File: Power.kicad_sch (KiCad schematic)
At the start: 74 parts, among them J10 Conn_01x02_Socket, J12 USB_C_Receptacle_USB2.0_14P, J22 Conn_01x02_Socket, J23 Conn_01x02_Socket, J24 Conn_01x02_Socket, J25 Conn_01x02_Socket, Q1 NMOS, Q6 NMOS, Q7 NMOS, U10 INA219AxD, U11 TLV62569ADRL, U12 USBLC6-2P6, U15 TPS60400DBV, U17 TCPP03-M20, U4 TPS513885VABR, U9 INA219AxD

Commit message: adding footprins to usbpd
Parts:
- Q6, Q7: footprint (none) -> Package_TO_SOT_SMD:TSOT-23
- R64, R65: footprint (none) -> Resistor_SMD:R_0603_1608Metric
- R66: footprint (none) -> Resistor_SMD:R_1206_3216Metric
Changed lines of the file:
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@@
 			)
 		)
-		(property "Footprint" ""
+		(property "Footprint" "Package_TO_SOT_SMD:TSOT-23"
 			(at 285.75 166.37 0)
 			(hide yes)
@@
 			)
 		)
-		(property "Description" "N-MOSFET transistor, drain/source/gate"
+		(property "Description" "RQ6C050UNTR"
 			(at 288.29 171.45 0)
 			(hide yes)
@@
 			)
 		)
-		(property "Footprint" ""
+		(property "Footprint" "Package_TO_SOT_SMD:TSOT-23"
 			(at 304.8 166.37 0)
 			(hide yes)
@@
 			)
 		)
-		(property "Description" "N-MOSFET transistor, drain/source/gate"
+		(property "Description" "RQ6C050UNTR"
 			(at 302.26 171.45 0)
 			(hide yes)
@@
 			)
 		)
-		(property "Footprint" ""
+		(property "Footprint" "Resistor_SMD:R_1206_3216Metric"
 			(at 240.03 170.688 90)
 			(hide yes)
@@
 			)
 		)
-		(property "Footprint" ""
+		(property "Footprint" "Resistor_SMD:R_0603_1608Metric"
 			(at 239.522 189.23 90)
 			(hide yes)
@@
 			)
 		)
-		(property "Footprint" ""
+		(property "Footprint" "Resistor_SMD:R_0603_1608Metric"
 			(at 239.522 203.2 90)
 			(hide yes)

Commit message: figuring out startup for usbpd
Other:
- note added: "20V to 5V Buck Converter"
- note removed: "20V-5V Buck Converter"
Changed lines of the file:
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@@
 		)
 	)
-	(text "20V-5V Buck Converter"
+	(text "20V to 5V Buck Converter"
 		(exclude_from_sim no)
 		(at 142.24 89.662 0)

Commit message: Buck work
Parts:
- added C66, C72, C79: 100n, Package_TO_SOT_SMD:SOT-23-6, symbol Device:C
- added C73, C74, C75: C, Package_TO_SOT_SMD:SOT-23-6, symbol Device:C
- added C76, C78: DNP, Package_TO_SOT_SMD:SOT-23-6, symbol Device:C
- added C77: 15u, Package_TO_SOT_SMD:SOT-23-6, symbol Device:C
- added D11: LED, LED_SMD:LED_0603_1608Metric, symbol Device:LED
- added L3: L, symbol Device:L
- added R46, R67: R, symbol Device:R
- added R77: 330, Resistor_SMD:R_0603_1608Metric, symbol Device:R
- added U18: TPS54302, Package_TO_SOT_SMD:SOT-23-6, symbol Regulator_Switching:TPS54302
- C57: value 100nF -> 100n
- C60: value 2.2u -> 2u2
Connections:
- net +20V: no longer C61.1, C62.1, C63.1, C64.1, Q7.1 (D), U4.1 (VIN)
- net 3V3: now also C73.1, C74.1, C75.1, C76.1, C79.1, L3.2, R46.1, R77.1
- net GND: now also C72.2, C74.2, C75.2, C76.2, C77.2, C78.2, C79.2, D11.1 (K), R67.2, U18.1 (GND)
- new net: C66.2, L3.1, U18.2 (SW)
- new net: C73.2, R46.2, R67.1, U18.4 (FB)
- new net: C66.1, U18.6 (BOOT)
- new net: D11.2 (A), R77.2
- new net 20V: C61.1, C62.1, C63.1, C64.1, C72.1, C77.1, C78.1, Q7.1 (D), U18.3 (VIN), U4.1 (VIN)
- no-connect marks 4 -> 5
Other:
- note added: "BUCK CONVERTER 5V/20V-3V3"
- note added: "TI WeBench:"
- moved on the sheet: R64, R65

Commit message: update
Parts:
- added R86: DNP, symbol Device:R
- C74: value C -> 47u
- L3: value L -> 10u
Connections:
- net 20V: now also R86.2
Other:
- note added: "Dev Board Link"
- note added: "TI WeBench: https://webench.ti.com/power-designer/switching-regulator/customize/40"
- note removed: "TI WeBench:"
- moved on the sheet: C72, C77

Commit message: PWR
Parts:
- added R87: 2m, Resistor_SMD:R_0603_1608Metric, symbol Device:R
- added R88: 0R, Resistor_SMD:R_1210_3225Metric_Pad1.30x2.65mm_HandSolder, symbol Device:R
- C73: value C -> 82p
- C75: value C -> 100n
- C79: value 100n -> DNP
- R46: value R -> 100k
- R67: value R -> 22k
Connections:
- net 20V: now also R88.1; no longer C72.1, C77.1, C78.1, R86.2, U18.3 (VIN)
- net 3V3: now also R87.2; no longer C73.1, C74.1, C75.1, C76.1, C79.1, L3.2, R46.1
- net 3V3_AMPS_1: now also C73.1, C74.1, C75.1, C76.1, C79.1, L3.2, R46.1, R87.1
- net VBUS_STM: now also R86.1
- new net: C72.1, C77.1, C78.1, R86.2, R88.2, U18.3 (VIN)
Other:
- moved on the sheet: C20, C21, C30, C31, C51, C54, C55, C56, C57, C58, C59, C60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

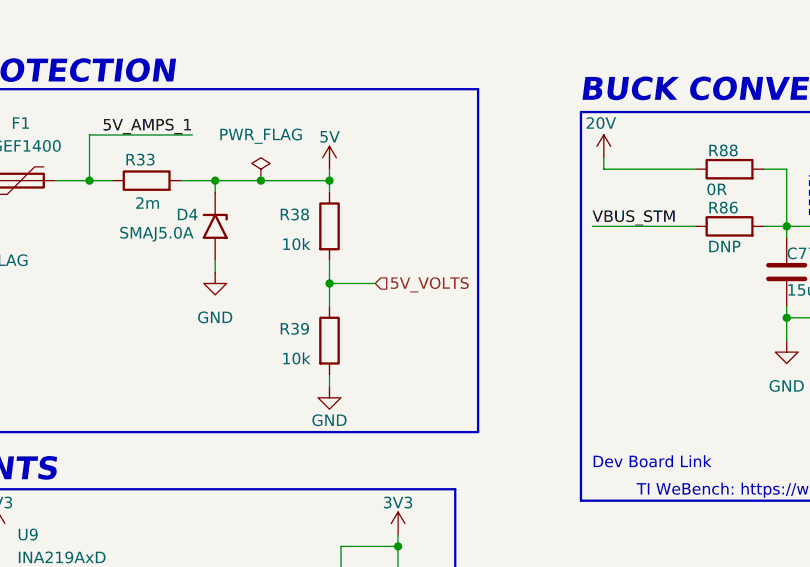
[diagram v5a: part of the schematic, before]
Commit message: getting rid of 5V check
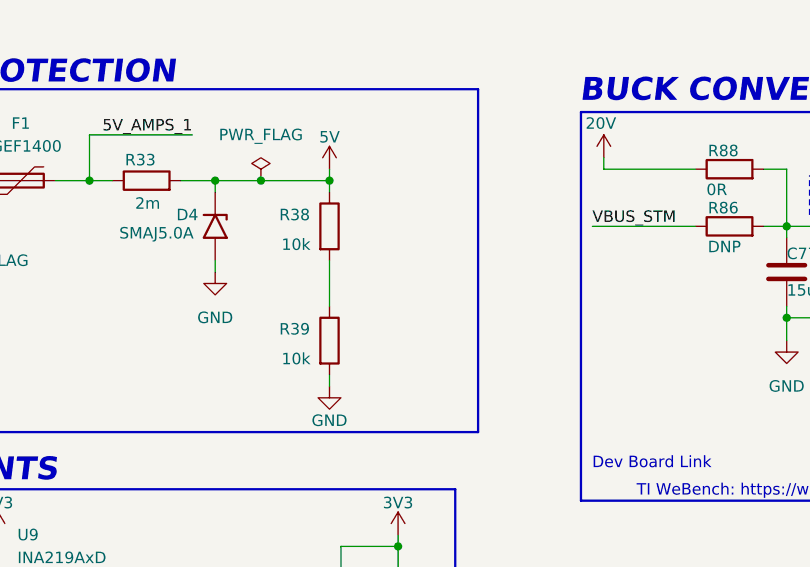
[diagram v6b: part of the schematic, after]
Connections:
- net 5V_VOLTS: no longer names the net of R38.2, R39.1
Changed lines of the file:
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@@
 	)
 	(junction
-		(at 86.36 44.45)
-		(diameter 0)
-		(color 0 0 0 0)
-	)
-	(junction
 		(at 223.52 40.64)
 		(diameter 0)
@@
 	(wire
 		(pts
-			(xy 86.36 41.91) (xy 86.36 44.45)
+			(xy 86.36 41.91) (xy 86.36 46.99)
 		)
 		(stroke
@@
 	(wire
 		(pts
-			(xy 86.36 44.45) (xy 86.36 46.99)
-		)
-		(stroke
-			(width 0)
-			(type default)
-		)
-	)
-	(wire
-		(pts
 			(xy 218.44 166.37) (xy 218.44 168.91)
 		)
@@
 	(wire
 		(pts
-			(xy 86.36 44.45) (xy 91.44 44.45)
-		)
-		(stroke
-			(width 0)
-			(type default)
-		)
-	)
-	(wire
-		(pts
 			(xy 128.27 209.55) (xy 128.27 207.01)
 		)
@@
 		(effects
 			(font
-				(size 1.27 1.27)
-			)
-			(justify left)
-		)
-	)
-	(hierarchical_label "5V_VOLTS"
-		(shape input)
-		(at 91.44 44.45 0)
-		(effects
-			(font

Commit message: PWR
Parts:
- removed C20: 4u7, Capacitor_SMD:C_0603_1608Metric, symbol Device:C
- removed C21: 22u, Capacitor_SMD:C_0603_1608Metric, symbol Device:C
- removed C51, C54, C55: DNP, Capacitor_SMD:C_0603_1608Metric, symbol Device:C
- removed D10: D, Diode_SMD:D_1206_3216Metric, symbol Device:D
- removed D5: LED, LED_SMD:LED_0603_1608Metric, symbol Device:LED
- removed L1: 1u, Inductor_SMD:L_Bourns-SRN8040_8x8.15mm, symbol Device:L
- removed R40: 453k, Resistor_SMD:R_0603_1608Metric, symbol Device:R
- removed R41: 100k, Resistor_SMD:R_0603_1608Metric, symbol Device:R
- removed R42: 2m, Resistor_SMD:R_0603_1608Metric, symbol Device:R
- removed R43: 330, Resistor_SMD:R_0603_1608Metric, symbol Device:R
- removed U11: TLV62569ADRL, Package_TO_SOT_SMD:SOT-563, symbol Regulator_Switching:TLV62569ADRL
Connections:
- net 5V_VOLTS: now reaches R38.2, R39.1
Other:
- note removed: "BUCK CONVERTER 5V-3.3V"
- note removed: "https://webench.ti.com/power-designer/switching-regulator/export/12?noparams=0"

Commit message: Buck footprints
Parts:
- C66, C72, C73, C75, C79: footprint Package_TO_SOT_SMD:SOT-23-6 -> Capacitor_SMD:C_0603_1608Metric_Pad1.08x0.95mm_HandSolder
- C74, C76, C77: footprint Package_TO_SOT_SMD:SOT-23-6 -> Capacitor_SMD:C_1210_3225Metric
- L3: footprint (none) -> Inductor_SMD:L_12x12mm_H6mm
- R46, R67: footprint (none) -> Resistor_SMD:R_0603_1608Metric
- R86: footprint (none) -> Resistor_SMD:R_1210_3225Metric_Pad1.30x2.65mm_HandSolder
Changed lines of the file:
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@@
 			)
 		)
-		(property "Footprint" "Package_TO_SOT_SMD:SOT-23-6"
+		(property "Footprint" "Capacitor_SMD:C_0603_1608Metric_Pad1.08x0.95mm_HandSolder"
 			(at 224.4852 49.53 0)
 			(hide yes)
@@
 			)
 		)
-		(property "Footprint" "Package_TO_SOT_SMD:SOT-23-6"
+		(property "Footprint" "Capacitor_SMD:C_0603_1608Metric_Pad1.08x0.95mm_HandSolder"
 			(at 219.4052 49.53 0)
 			(hide yes)
@@
 			)
 		)
-		(property "Footprint" "Package_TO_SOT_SMD:SOT-23-6"
+		(property "Footprint" "Capacitor_SMD:C_1210_3225Metric"
 			(at 138.1252 46.99 0)
 			(hide yes)
@@
 			)
 		)
-		(property "Footprint" "Package_TO_SOT_SMD:SOT-23-6"
+		(property "Footprint" "Capacitor_SMD:C_0603_1608Metric_Pad1.08x0.95mm_HandSolder"
 			(at 143.2052 46.99 0)
 			(hide yes)
@@
 			)
 		)
-		(property "Footprint" ""
+		(property "Footprint" "Resistor_SMD:R_1210_3225Metric_Pad1.30x2.65mm_HandSolder"
 			(at 130.81 39.878 90)
 			(hide yes)
@@
 			)
 		)
-		(property "Footprint" ""
+		(property "Footprint" "Resistor_SMD:R_0603_1608Metric"
 			(at 195.072 45.72 90)
 			(hide yes)
@@
 			)
 		)
-		(property "Footprint" "Package_TO_SOT_SMD:SOT-23-6"
+		(property "Footprint" "Capacitor_SMD:C_1210_3225Metric"
 			(at 229.5652 49.53 0)
 			(hide yes)
@@
 			)
 		)
-		(property "Footprint" ""
+		(property "Footprint" "Inductor_SMD:L_12x12mm_H6mm"
 			(at 191.77 40.64 0)
 			(hide yes)
@@
 			)
 		)
-		(property "Footprint" "Package_TO_SOT_SMD:SOT-23-6"
+		(property "Footprint" "Capacitor_SMD:C_0603_1608Metric_Pad1.08x0.95mm_HandSolder"
 			(at 182.88 37.1348 0)
 			(hide yes)
@@
 			)
 		)
-		(property "Footprint" ""
+		(property "Footprint" "Resistor_SMD:R_0603_1608Metric"
 			(at 195.072 57.15 90)
 			(hide yes)
@@
 			)
 		)
-		(property "Footprint" "Package_TO_SOT_SMD:SOT-23-6"
+		(property "Footprint" "Capacitor_SMD:C_1210_3225Metric"
 			(at 214.3252 49.53 0)
 			(hide yes)
@@
 			)
 		)
-		(property "Footprint" "Package_TO_SOT_SMD:SOT-23-6"
+		(property "Footprint" "Capacitor_SMD:C_0603_1608Metric_Pad1.08x0.95mm_HandSolder"
 			(at 206.7052 49.53 0)
 			(hide yes)
